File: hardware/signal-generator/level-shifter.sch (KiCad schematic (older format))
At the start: 27 parts

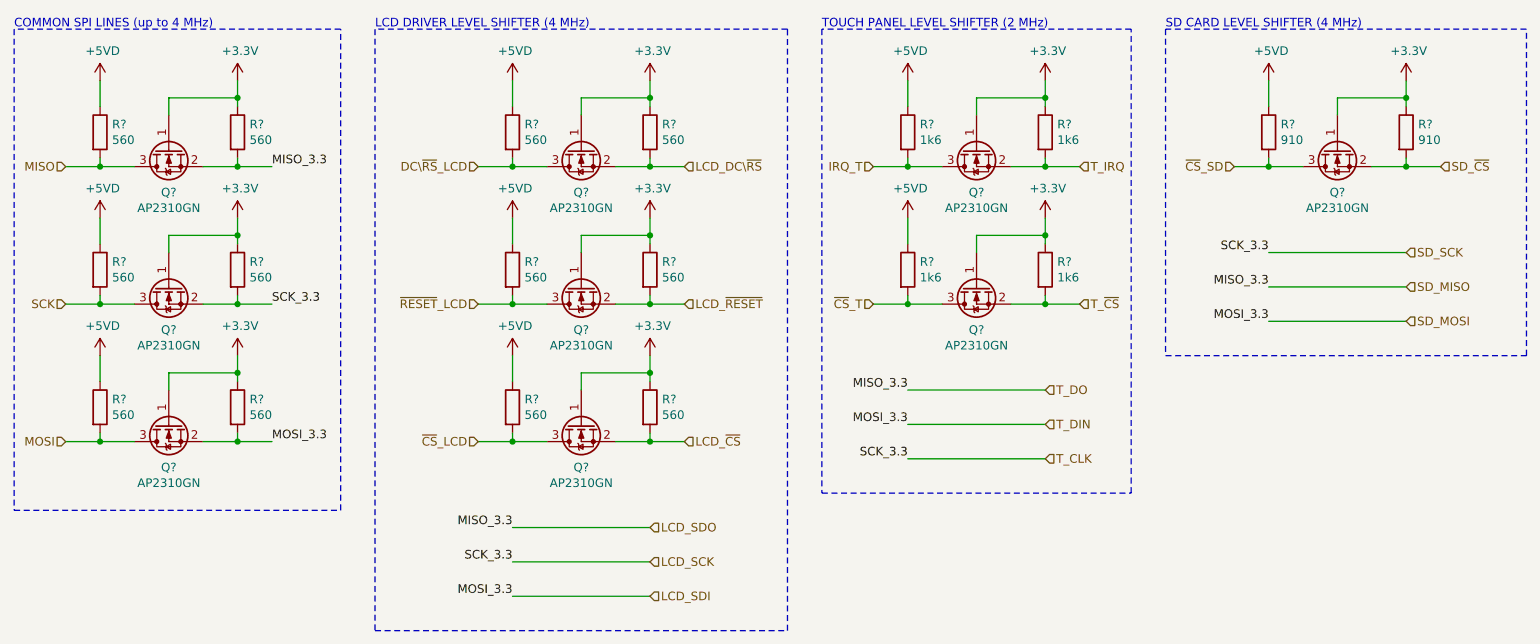
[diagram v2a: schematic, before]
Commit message: [Signal Generator] Implement +3.3VD line with TC1017 voltage regulator
Up until now, the +3.3VD line was implemented using the L78L33 linear
voltage regulator. However, the latter has a dropout voltage of 2V which
means that the L78L33 cannot output a stable +3.3V from a +5V input.

To solve the aforementioned problem the TC1017 LDO voltage regulator has
replaced the L78L33. The former has a low dropout voltage of 180mV (typ.) at
100mA load current.
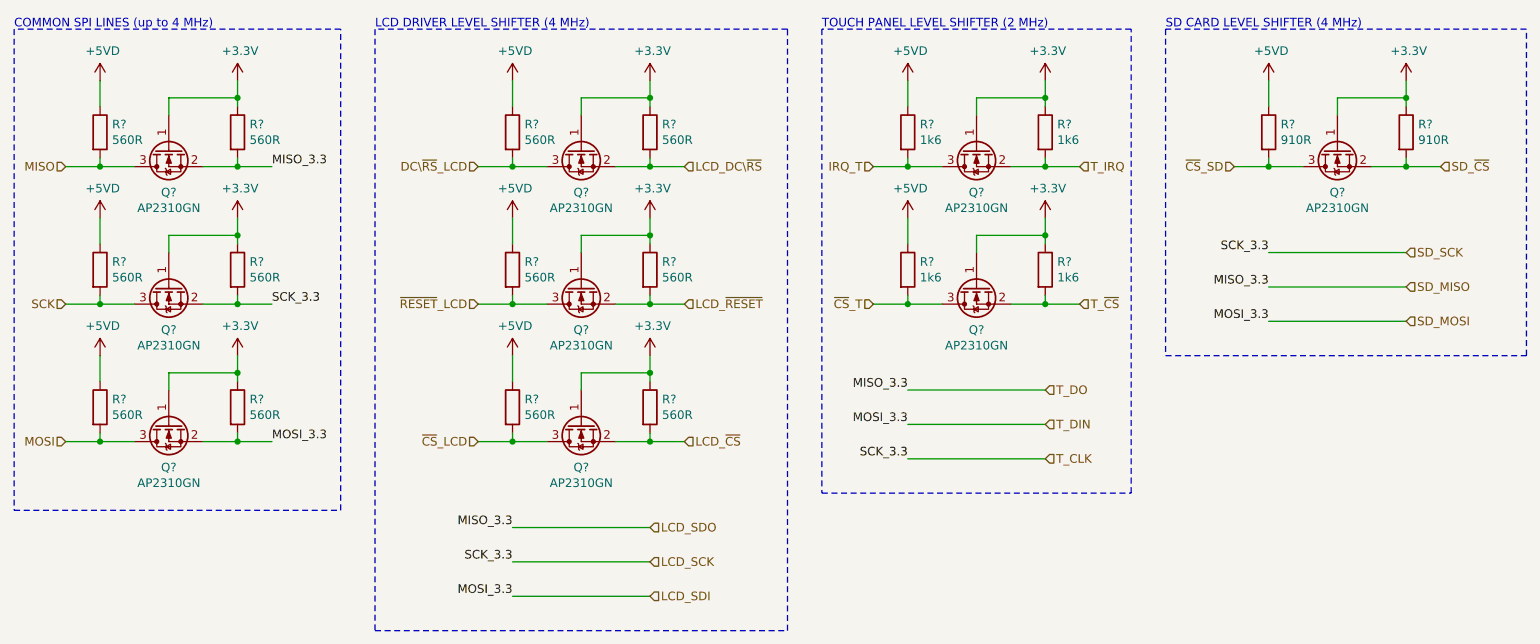
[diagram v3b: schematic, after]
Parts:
- R? (x12): value 560 -> 560R; footprint (none) -> Resistors_SMD:R_1206_HandSoldering
- R? (x2): value 910 -> 910R; footprint (none) -> Resistors_SMD:R_1206_HandSoldering
- R? (x4): footprint (none) -> Resistors_SMD:R_1206_HandSoldering
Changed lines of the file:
@@
 P 9900 1750
 F 0 "R?" H 9970 1796 50  0000 L CNN
-F 1 "910" H 9970 1705 50  0000 L CNN
-F 2 "" V 9830 1750 50  0001 C CNN
+F 1 "910R" H 9970 1705 50  0000 L CNN
+F 2 "Resistors_SMD:R_1206_HandSoldering" V 9830 1750 50  0001 C CNN
 F 3 "~" H 9900 1750 50  0001 C CNN
 	1    9900 1750
@@
 P 9100 1750
 F 0 "R?" H 9170 1796 50  0000 L CNN
-F 1 "910" H 9170 1705 50  0000 L CNN
-F 2 "" V 9030 1750 50  0001 C CNN
+F 1 "910R" H 9170 1705 50  0000 L CNN
+F 2 "Resistors_SMD:R_1206_HandSoldering" V 9030 1750 50  0001 C CNN
 F 3 "~" H 9100 1750 50  0001 C CNN
 	1    9100 1750
@@
 Connection ~ 9100 1950
 $Comp
-L power:+3.3V #PWR?
+L power:+3.3V #PWR0228
 U 1 1 5DE29376
 P 9900 1450
-F 0 "#PWR?" H 9900 1300 50  0001 C CNN
+F 0 "#PWR0228" H 9900 1300 50  0001 C CNN
 F 1 "+3.3V" H 9915 1623 50  0000 C CNN
 F 2 "" H 9900 1450 50  0001 C CNN
@@
 $EndComp
 $Comp
-L power:+5VD #PWR?
+L power:+5VD #PWR0229
 U 1 1 5DE2937C
 P 9100 1450
-F 0 "#PWR?" H 9100 1300 50  0001 C CNN
+F 0 "#PWR0229" H 9100 1300 50  0001 C CNN
 F 1 "+5VD" H 9115 1623 50  0000 C CNN
 F 2 "" H 9100 1450 50  0001 C CNN
@@
 F 0 "R?" H 7870 1796 50  0000 L CNN
 F 1 "1k6" H 7870 1705 50  0000 L CNN
-F 2 "" V 7730 1750 50  0001 C CNN
+F 2 "Resistors_SMD:R_1206_HandSoldering" V 7730 1750 50  0001 C CNN
 F 3 "~" H 7800 1750 50  0001 C CNN
 	1    7800 1750
@@
 F 0 "R?" H 7070 1796 50  0000 L CNN
 F 1 "1k6" H 7070 1705 50  0000 L CNN
-F 2 "" V 6930 1750 50  0001 C CNN
+F 2 "Resistors_SMD:R_1206_HandSoldering" V 6930 1750 50  0001 C CNN
 F 3 "~" H 7000 1750 50  0001 C CNN
 	1    7000 1750
@@
 Connection ~ 7000 1950
 $Comp
-L power:+3.3V #PWR?
+L power:+3.3V #PWR0230
 U 1 1 5DE2D71E
 P 7800 1450
-F 0 "#PWR?" H 7800 1300 50  0001 C CNN
+F 0 "#PWR0230" H 7800 1300 50  0001 C CNN
 F 1 "+3.3V" H 7815 1623 50  0000 C CNN
 F 2 "" H 7800 1450 50  0001 C CNN
@@
 $EndComp
 $Comp
-L power:+5VD #PWR?
+L power:+5VD #PWR0231
 U 1 1 5DE2D724
 P 7000 1450
-F 0 "#PWR?" H 7000 1300 50  0001 C CNN
+F 0 "#PWR0231" H 7000 1300 50  0001 C CNN
 F 1 "+5VD" H 7015 1623 50  0000 C CNN
 F 2 "" H 7000 1450 50  0001 C CNN
@@
 F 0 "R?" H 7870 2596 50  0000 L CNN
 F 1 "1k6" H 7870 2505 50  0000 L CNN
-F 2 "" V 7730 2550 50  0001 C CNN
+F 2 "Resistors_SMD:R_1206_HandSoldering" V 7730 2550 50  0001 C CNN
 F 3 "~" H 7800 2550 50  0001 C CNN
 	1    7800 2550
@@
 F 0 "R?" H 7070 2596 50  0000 L CNN
 F 1 "1k6" H 7070 2505 50  0000 L CNN
-F 2 "" V 6930 2550 50  0001 C CNN
+F 2 "Resistors_SMD:R_1206_HandSoldering" V 6930 2550 50  0001 C CNN
 F 3 "~" H 7000 2550 50  0001 C CNN
 	1    7000 2550
@@
 Connection ~ 7000 2750
 $Comp
-L power:+3.3V #PWR?
+L power:+3.3V #PWR0232
 U 1 1 5DE2D7AE
 P 7800 2250
-F 0 "#PWR?" H 7800 2100 50  0001 C CNN
+F 0 "#PWR0232" H 7800 2100 50  0001 C CNN
 F 1 "+3.3V" H 7815 2423 50  0000 C CNN
 F 2 "" H 7800 2250 50  0001 C CNN
@@
 $EndComp
 $Comp
-L power:+5VD #PWR?
+L power:+5VD #PWR0233
 U 1 1 5DE2D7B4
 P 7000 2250
-F 0 "#PWR?" H 7000 2100 50  0001 C CNN
+F 0 "#PWR0233" H 7000 2100 50  0001 C CNN
 F 1 "+5VD" H 7015 2423 50  0000 C CNN
 F 2 "" H 7000 2250 50  0001 C CNN
@@
 P 3100 1750
 F 0 "R?" H 3170 1796 50  0000 L CNN
-F 1 "560" H 3170 1705 50  0000 L CNN
-F 2 "" V 3030 1750 50  0001 C CNN
+F 1 "560R" H 3170 1705 50  0000 L CNN
+F 2 "Resistors_SMD:R_1206_HandSoldering" V 3030 1750 50  0001 C CNN
 F 3 "~" H 3100 1750 50  0001 C CNN
 	1    3100 1750
@@
 P 2300 1750
 F 0 "R?" H 2370 1796 50  0000 L CNN
-F 1 "560" H 2370 1705 50  0000 L CNN
-F 2 "" V 2230 1750 50  0001 C CNN
+F 1 "560R" H 2370 1705 50  0000 L CNN
+F 2 "Resistors_SMD:R_1206_HandSoldering" V 2230 1750 50  0001 C CNN
 F 3 "~" H 2300 1750 50  0001 C CNN
 	1    2300 1750
@@
 Connection ~ 2300 1950
 $Comp
-L power:+3.3V #PWR?
+L power:+3.3V #PWR0234
 U 1 1 5DDC7797
 P 3100 1450
-F 0 "#PWR?" H 3100 1300 50  0001 C CNN
+F 0 "#PWR0234" H 3100 1300 50  0001 C CNN
 F 1 "+3.3V" H 3115 1623 50  0000 C CNN
 F 2 "" H 3100 1450 50  0001 C CNN
@@
 $EndComp
 $Comp
-L power:+5VD #PWR?
+L power:+5VD #PWR0235
 U 1 1 5DDC779D
 P 2300 1450
-F 0 "#PWR?" H 2300 1300 50  0001 C CNN
+F 0 "#PWR0235" H 2300 1300 50  0001 C CNN
 F 1 "+5VD" H 2315 1623 50  0000 C CNN
 F 2 "" H 2300 1450 50  0001 C CNN
@@
 P 3100 2550
 F 0 "R?" H 3170 2596 50  0000 L CNN
-F 1 "560" H 3170 2505 50  0000 L CNN
-F 2 "" V 3030 2550 50  0001 C CNN
+F 1 "560R" H 3170 2505 50  0000 L CNN
+F 2 "Resistors_SMD:R_1206_HandSoldering" V 3030 2550 50  0001 C CNN
 F 3 "~" H 3100 2550 50  0001 C CNN
 	1    3100 2550
@@
 P 2300 2550
 F 0 "R?" H 2370 2596 50  0000 L CNN
-F 1 "560" H 2370 2505 50  0000 L CNN
-F 2 "" V 2230 2550 50  0001 C CNN
+F 1 "560R" H 2370 2505 50  0000 L CNN
+F 2 "Resistors_SMD:R_1206_HandSoldering" V 2230 2550 50  0001 C CNN
 F 3 "~" H 2300 2550 50  0001 C CNN
 	1    2300 2550
@@
 Connection ~ 2300 2750
 $Comp
-L power:+3.3V #PWR?
+L power:+3.3V #PWR0236
 U 1 1 5DDC77C6
 P 3100 2250
-F 0 "#PWR?" H 3100 2100 50  0001 C CNN
+F 0 "#PWR0236" H 3100 2100 50  0001 C CNN
 F 1 "+3.3V" H 3115 2423 50  0000 C CNN
 F 2 "" H 3100 2250 50  0001 C CNN
@@
 $EndComp
 $Comp
-L power:+5VD #PWR?
+L power:+5VD #PWR0237
 U 1 1 5DDC77CC
 P 2300 2250
-F 0 "#PWR?" H 2300 2100 50  0001 C CNN
+F 0 "#PWR0237" H 2300 2100 50  0001 C CNN
 F 1 "+5VD" H 2315 2423 50  0000 C CNN
 F 2 "" H 2300 2250 50  0001 C CNN
@@
 P 3100 3350
 F 0 "R?" H 3170 3396 50  0000 L CNN
-F 1 "560" H 3170 3305 50  0000 L CNN
-F 2 "" V 3030 3350 50  0001 C CNN
+F 1 "560R" H 3170 3305 50  0000 L CNN
+F 2 "Resistors_SMD:R_1206_HandSoldering" V 3030 3350 50  0001 C CNN
 F 3 "~" H 3100 3350 50  0001 C CNN
 	1    3100 3350
@@
 P 2300 3350
 F 0 "R?" H 2370 3396 50  0000 L CNN
-F 1 "560" H 2370 3305 50  0000 L CNN
-F 2 "" V 2230 3350 50  0001 C CNN
+F 1 "560R" H 2370 3305 50  0000 L CNN
+F 2 "Resistors_SMD:R_1206_HandSoldering" V 2230 3350 50  0001 C CNN
 F 3 "~" H 2300 3350 50  0001 C CNN
 	1    2300 3350
@@
 Connection ~ 2300 3550
 $Comp
-L power:+3.3V #PWR?
+L power:+3.3V #PWR0238
 U 1 1 5DDC77F5
 P 3100 3050
-F 0 "#PWR?" H 3100 2900 50  0001 C CNN
+F 0 "#PWR0238" H 3100 2900 50  0001 C CNN
 F 1 "+3.3V" H 3115 3223 50  0000 C CNN
 F 2 "" H 3100 3050 50  0001 C CNN
@@
 $EndComp
 $Comp
-L power:+5VD #PWR?
+L power:+5VD #PWR0239
 U 1 1 5DDC77FB
 P 2300 3050
-F 0 "#PWR?" H 2300 2900 50  0001 C CNN
+F 0 "#PWR0239" H 2300 2900 50  0001 C CNN
 F 1 "+5VD" H 2315 3223 50  0000 C CNN
 F 2 "" H 2300 3050 50  0001 C CNN
@@
 P 5500 1750
 F 0 "R?" H 5570 1796 50  0000 L CNN
-F 1 "560" H 5570 1705 50  0000 L CNN
-F 2 "" V 5430 1750 50  0001 C CNN
+F 1 "560R" H 5570 1705 50  0000 L CNN
+F 2 "Resistors_SMD:R_1206_HandSoldering" V 5430 1750 50  0001 C CNN
 F 3 "~" H 5500 1750 50  0001 C CNN
 	1    5500 1750
@@
 P 4700 1750
 F 0 "R?" H 4770 1796 50  0000 L CNN
-F 1 "560" H 4770 1705 50  0000 L CNN
-F 2 "" V 4630 1750 50  0001 C CNN
+F 1 "560R" H 4770 1705 50  0000 L CNN
+F 2 "Resistors_SMD:R_1206_HandSoldering" V 4630 1750 50  0001 C CNN
 F 3 "~" H 4700 1750 50  0001 C CNN
 	1    4700 1750
@@
 Connection ~ 4700 1950
 $Comp
-L power:+3.3V #PWR?
+L power:+3.3V #PWR0240
 U 1 1 5DDC7824
 P 5500 1450
-F 0 "#PWR?" H 5500 1300 50  0001 C CNN
+F 0 "#PWR0240" H 5500 1300 50  0001 C CNN
 F 1 "+3.3V" H 5515 1623 50  0000 C CNN
 F 2 "" H 5500 1450 50  0001 C CNN
@@
 $EndComp
 $Comp
-L power:+5VD #PWR?
+L power:+5VD #PWR0241
 U 1 1 5DDC782A
 P 4700 1450
-F 0 "#PWR?" H 4700 1300 50  0001 C CNN
+F 0 "#PWR0241" H 4700 1300 50  0001 C CNN
 F 1 "+5VD" H 4715 1623 50  0000 C CNN
 F 2 "" H 4700 1450 50  0001 C CNN
@@
 P 5500 2550
 F 0 "R?" H 5570 2596 50  0000 L CNN
-F 1 "560" H 5570 2505 50  0000 L CNN
-F 2 "" V 5430 2550 50  0001 C CNN
+F 1 "560R" H 5570 2505 50  0000 L CNN
+F 2 "Resistors_SMD:R_1206_HandSoldering" V 5430 2550 50  0001 C CNN
 F 3 "~" H 5500 2550 50  0001 C CNN
 	1    5500 2550
@@
 P 4700 2550
 F 0 "R?" H 4770 2596 50  0000 L CNN
-F 1 "560" H 4770 2505 50  0000 L CNN
-F 2 "" V 4630 2550 50  0001 C CNN
+F 1 "560R" H 4770 2505 50  0000 L CNN
+F 2 "Resistors_SMD:R_1206_HandSoldering" V 4630 2550 50  0001 C CNN
 F 3 "~" H 4700 2550 50  0001 C CNN
 	1    4700 2550
@@
 Connection ~ 4700 2750
 $Comp
-L power:+3.3V #PWR?
+L power:+3.3V #PWR0242
 U 1 1 5DDC7853
 P 5500 2250
-F 0 "#PWR?" H 5500 2100 50  0001 C CNN
+F 0 "#PWR0242" H 5500 2100 50  0001 C CNN
 F 1 "+3.3V" H 5515 2423 50  0000 C CNN
 F 2 "" H 5500 2250 50  0001 C CNN
@@
 $EndComp
 $Comp
-L power:+5VD #PWR?
+L power:+5VD #PWR0243
 U 1 1 5DDC7859
 P 4700 2250
-F 0 "#PWR?" H 4700 2100 50  0001 C CNN
+F 0 "#PWR0243" H 4700 2100 50  0001 C CNN
 F 1 "+5VD" H 4715 2423 50  0000 C CNN
 F 2 "" H 4700 2250 50  0001 C CNN
@@
 P 5500 3350
 F 0 "R?" H 5570 3396 50  0000 L CNN
-F 1 "560" H 5570 3305 50  0000 L CNN
-F 2 "" V 5430 3350 50  0001 C CNN
+F 1 "560R" H 5570 3305 50  0000 L CNN
+F 2 "Resistors_SMD:R_1206_HandSoldering" V 5430 3350 50  0001 C CNN
 F 3 "~" H 5500 3350 50  0001 C CNN
 	1    5500 3350
@@
 P 4700 3350
 F 0 "R?" H 4770 3396 50  0000 L CNN
-F 1 "560" H 4770 3305 50  0000 L CNN
-F 2 "" V 4630 3350 50  0001 C CNN
+F 1 "560R" H 4770 3305 50  0000 L CNN
+F 2 "Resistors_SMD:R_1206_HandSoldering" V 4630 3350 50  0001 C CNN
 F 3 "~" H 4700 3350 50  0001 C CNN
 	1    4700 3350
@@
 Connection ~ 4700 3550
 $Comp
-L power:+3.3V #PWR?
+L power:+3.3V #PWR0244
 U 1 1 5DE5E994
 P 5500 3050
-F 0 "#PWR?" H 5500 2900 50  0001 C CNN
+F 0 "#PWR0244" H 5500 2900 50  0001 C CNN
 F 1 "+3.3V" H 5515 3223 50  0000 C CNN
 F 2 "" H 5500 3050 50  0001 C CNN
@@
 $EndComp
 $Comp
-L power:+5VD #PWR?
+L power:+5VD #PWR0245
 U 1 1 5DE5E99A
 P 4700 3050
-F 0 "#PWR?" H 4700 2900 50  0001 C CNN
+F 0 "#PWR0245" H 4700 2900 50  0001 C CNN
 F 1 "+5VD" H 4715 3223 50  0000 C CNN
 F 2 "" H 4700 3050 50  0001 C CNN
